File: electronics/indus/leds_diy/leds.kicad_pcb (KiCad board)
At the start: 2 copper layers, 230 x 35.6 mm, 21 parts, among them P1 LED+, P2 THERM, P3 LED-

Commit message: new connector footprint
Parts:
- P1, P3: footprint risebox:PINHEAD_LOCK_1-4 -> risebox:CONNECT_TE_3-647166-4
- P2: footprint risebox:PINHEAD_LOCK_1-3 -> risebox:CONNECT_TE_3-647166-3
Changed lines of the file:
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@@
   )
   (setup
-    (last_trace_width 0.8)
+    (last_trace_width 0.6)
     (user_trace_width 0.3)
     (user_trace_width 0.8)
@@
     )
   )
-  (module risebox:PINHEAD_LOCK_1-4 (layer F.Cu)
-    (at 45.1739 87.7443 270)
-    (attr virtual)
-    (fp_text reference P1 (at 0 -5 270) (layer F.SilkS)
-      (effects (font (size 1 1) (thickness 0.15)))
-    )
-    (fp_text value LED+ (at 0 5 270) (layer F.Fab)
-      (effects (font (size 1 1) (thickness 0.15)))
-    )
-    (fp_line (start -5.04 -1.675) (end 5.04 -1.675) (layer F.SilkS) (width 0.15))
-    (fp_line (start 5.04 2.54) (end -5.04 2.54) (layer F.SilkS) (width 0.15))
-    (fp_line (start -5.04 -3.175) (end 5.04 -3.175) (layer F.SilkS) (width 0.15))
-    (fp_line (start -5.04 -3.175) (end -5.04 2.54) (layer F.SilkS) (width 0.15))
-    (fp_line (start 5.04 -3.175) (end 5.04 2.54) (layer F.SilkS) (width 0.15))
-    (pad 4 thru_hole oval (at 3.77 0 270) (size 1.50622 3.01498) (drill 0.99822) (layers *.Cu *.Mask)
-      (net 8 "Net-(D4-Pad1)"))
-    (pad 3 thru_hole oval (at 1.27 0 270) (size 1.50622 3.01498) (drill 0.99822) (layers *.Cu *.Mask)
-      (net 6 "Net-(D3-Pad1)"))
-    (pad 1 thru_hole oval (at -3.77 0 270) (size 1.50622 3.01498) (drill 0.99822) (layers *.Cu *.Mask)
-      (net 2 "Net-(D1-Pad1)"))
-    (pad 2 thru_hole oval (at -1.23 0 270) (size 1.50622 3.01498) (drill 0.99822) (layers *.Cu *.Mask)
-      (net 4 "Net-(D2-Pad1)"))
-  )
-  (module risebox:PINHEAD_LOCK_1-4 (layer F.Cu)
-    (at 264.12 87.36 270)
-    (attr virtual)
-    (fp_text reference P3 (at 0 -5 270) (layer F.SilkS)
-      (effects (font (size 1 1) (thickness 0.15)))
-    )
-    (fp_text value LED- (at 0 5 270) (layer F.Fab)
-      (effects (font (size 1 1) (thickness 0.15)))
-    )
-    (fp_line (start -5.04 -1.675) (end 5.04 -1.675) (layer F.SilkS) (width 0.15))
-    (fp_line (start 5.04 2.54) (end -5.04 2.54) (layer F.SilkS) (width 0.15))
-    (fp_line (start -5.04 -3.175) (end 5.04 -3.175) (layer F.SilkS) (width 0.15))
-    (fp_line (start -5.04 -3.175) (end -5.04 2.54) (layer F.SilkS) (width 0.15))
-    (fp_line (start 5.04 -3.175) (end 5.04 2.54) (layer F.SilkS) (width 0.15))
-    (pad 4 thru_hole oval (at 3.77 0 270) (size 1.50622 3.01498) (drill 0.99822) (layers *.Cu *.Mask)
-      (net 17 "Net-(D13-Pad2)"))
-    (pad 3 thru_hole oval (at 1.27 0 270) (size 1.50622 3.01498) (drill 0.99822) (layers *.Cu *.Mask)
-      (net 18 "Net-(D14-Pad2)"))
-    (pad 1 thru_hole oval (at -3.77 0 270) (size 1.50622 3.01498) (drill 0.99822) (layers *.Cu *.Mask)
-      (net 20 "Net-(D16-Pad2)"))
-    (pad 2 thru_hole oval (at -1.23 0 270) (size 1.50622 3.01498) (drill 0.99822) (layers *.Cu *.Mask)
-      (net 19 "Net-(D15-Pad2)"))
-  )
   (module risebox:THERM_NTCS0603E3272JMT_SMD0603 (layer F.Cu)
     (at 110 148.9 90)
@@
       (net 21 GND))
   )
-  (module risebox:PINHEAD_LOCK_1-3 (layer F.Cu)
-    (at 74.8 139.4 90)
-    (attr virtual)
-    (fp_text reference P2 (at 0 -5 90) (layer F.SilkS)
-      (effects (font (size 1 1) (thickness 0.15)))
-    )
-    (fp_text value THERM (at 0 5 90) (layer F.Fab)
-      (effects (font (size 1 1) (thickness 0.15)))
-    )
-    (fp_line (start -3.84 -1.675) (end 3.84 -1.675) (layer F.SilkS) (width 0.15))
-    (fp_line (start 3.84 2.54) (end -3.84 2.54) (layer F.SilkS) (width 0.15))
-    (fp_line (start -3.84 -3.175) (end 3.84 -3.175) (layer F.SilkS) (width 0.15))
-    (fp_line (start -3.84 -3.175) (end -3.84 2.54) (layer F.SilkS) (width 0.15))
-    (fp_line (start 3.84 -3.175) (end 3.84 2.54) (layer F.SilkS) (width 0.15))
-    (pad 3 thru_hole oval (at 2.54 0 90) (size 1.50622 3.01498) (drill 0.99822) (layers *.Cu *.Mask)
-      (net 23 "Net-(P2-Pad3)"))
-    (pad 1 thru_hole oval (at -2.54 0 90) (size 1.50622 3.01498) (drill 0.99822) (layers *.Cu *.Mask)
-      (net 21 GND))
-    (pad 2 thru_hole oval (at 0 0 90) (size 1.50622 3.01498) (drill 0.99822) (layers *.Cu *.Mask)
-      (net 22 "Net-(P2-Pad2)"))
-  )
   (module risebox:LUXEON-C (layer F.Cu)
     (at 73.9942 85.4897)
@@
       (net 16 "Net-(D12-Pad2)") (solder_mask_margin 0.05) (solder_paste_margin -0.05))
   )
+  (module risebox:CONNECT_TE_3-647166-4 (layer F.Cu)
+    (at 45.1739 87.7443 270)
+    (fp_text reference P1 (at 0.05 8.4 270) (layer F.SilkS)
+      (effects (font (size 1 1) (thickness 0.15)))
+    )
+    (fp_text value LED+ (at 0.05 -6.7 270) (layer F.Fab)
+      (effects (font (size 1 1) (thickness 0.15)))
+    )
+    (fp_line (start 5.08 -3.175) (end 5.08 3.175) (layer F.SilkS) (width 0.15))
+    (fp_line (start -5.08 -3.175) (end -5.08 3.175) (layer F.SilkS) (width 0.15))
+    (fp_line (start -5.08 3.175) (end 5.08 3.175) (layer F.SilkS) (width 0.15))
+    (fp_line (start -5.08 -3.175) (end 5.08 -3.175) (layer F.SilkS) (width 0.15))
+    (pad 4 smd rect (at 3.81 -1.465 270) (size 1.78 5.97) (layers F.Cu F.Paste F.Mask)
+      (net 8 "Net-(D4-Pad1)"))
+    (pad 1 smd rect (at -3.81 1.465 270) (size 1.78 5.97) (layers F.Cu F.Paste F.Mask)
+      (net 2 "Net-(D1-Pad1)"))
+    (pad 3 smd rect (at 1.27 1.465 270) (size 1.78 5.97) (layers F.Cu F.Paste F.Mask)
+      (net 6 "Net-(D3-Pad1)"))
+    (pad 2 smd rect (at -1.27 -1.465 270) (size 1.78 5.97) (layers F.Cu F.Paste F.Mask)
+      (net 4 "Net-(D2-Pad1)"))
+  )
+  (module risebox:CONNECT_TE_3-647166-3 (layer F.Cu)
+    (at 74.8 139.4 90)
+    (fp_text reference P2 (at 0.05 8.4 90) (layer F.SilkS)
+      (effects (font (size 1 1) (thickness 0.15)))
+    )
+    (fp_text value THERM (at 0.05 -6.7 90) (layer F.Fab)
+      (effects (font (size 1 1) (thickness 0.15)))
+    )
+    (fp_line (start 3.81 -3.175) (end 3.81 3.175) (layer F.SilkS) (width 0.15))
+    (fp_line (start -3.81 -3.175) (end -3.81 3.175) (layer F.SilkS) (width 0.15))
+    (fp_line (start -3.81 3.175) (end 3.81 3.175) (layer F.SilkS) (width 0.15))
+    (fp_line (start -3.81 -3.175) (end 3.81 -3.175) (layer F.SilkS) (width 0.15))
+    (pad 1 smd rect (at -2.54 1.465 90) (size 1.78 5.97) (layers F.Cu F.Paste F.Mask)
+      (net 21 GND))
+    (pad 3 smd rect (at 2.54 1.465 90) (size 1.78 5.97) (layers F.Cu F.Paste F.Mask)
+      (net 23 "Net-(P2-Pad3)"))
+    (pad 2 smd rect (at 0 -1.465 90) (size 1.78 5.97) (layers F.Cu F.Paste F.Mask)
+      (net 22 "Net-(P2-Pad2)"))
+  )
+  (module risebox:CONNECT_TE_3-647166-4 (layer F.Cu)
+    (at 264.12 87.36 270)
+    (fp_text reference P3 (at 0.05 8.4 270) (layer F.SilkS)
+      (effects (font (size 1 1) (thickness 0.15)))
+    )
+    (fp_text value LED- (at 0.05 -6.7 270) (layer F.Fab)
+      (effects (font (size 1 1) (thickness 0.15)))
+    )
+    (fp_line (start 5.08 -3.175) (end 5.08 3.175) (layer F.SilkS) (width 0.15))
+    (fp_line (start -5.08 -3.175) (end -5.08 3.175) (layer F.SilkS) (width 0.15))
+    (fp_line (start -5.08 3.175) (end 5.08 3.175) (layer F.SilkS) (width 0.15))
+    (fp_line (start -5.08 -3.175) (end 5.08 -3.175) (layer F.SilkS) (width 0.15))
+    (pad 4 smd rect (at 3.81 -1.465 270) (size 1.78 5.97) (layers F.Cu F.Paste F.Mask)
+      (net 17 "Net-(D13-Pad2)"))
+    (pad 1 smd rect (at -3.81 1.465 270) (size 1.78 5.97) (layers F.Cu F.Paste F.Mask)
+      (net 20 "Net-(D16-Pad2)"))
+    (pad 3 smd rect (at 1.27 1.465 270) (size 1.78 5.97) (layers F.Cu F.Paste F.Mask)
+      (net 18 "Net-(D14-Pad2)"))
+    (pad 2 smd rect (at -1.27 -1.465 270) (size 1.78 5.97) (layers F.Cu F.Paste F.Mask)
+      (net 19 "Net-(D15-Pad2)"))
+  )
   (gr_line (start 71.2674 87.3984) (end 305.2674 87.3984) (angle 90) (layer F.SilkS) (width 0.2))

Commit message: 2 last LEDs well positioned on PCB
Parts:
- moved D9 55.0 mm to (184.3, 85.4)
- moved D10 50.3 mm to (180.0, 85.4)
- moved D12 49.9 mm to (184.3, 89.7)
- moved D11 48.0 mm to (180.0, 89.7)
- moved D16 32.0 mm to (238.2, 89.6)
- moved D15 23.0 mm to (233.9, 89.7)
- moved D14 14.0 mm to (233.9, 85.4)
- moved D13 5.91 mm to (238.2, 85.4)
- moved P1 0.58 mm to (45.7, 87.5)
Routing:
- net Net-(D2-Pad1): track 24.2 -> 22.4 mm
- net Net-(D3-Pad1): track 29.5 -> 29.0 mm
- net Net-(D1-Pad1): track 32.1 -> 31.6 mm
- net Net-(D4-Pad1): track 25.4 -> 24.9 mm
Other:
- board size 230 x 35.6 mm -> 230 x 35 mm

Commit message: fini routage LEDS
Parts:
- moved TH1 92.0 mm to (52.8, 76.9)
- moved R1 88.3 mm to (50.5, 71.6), turned to 0 degrees
- moved P2 68.9 mm to (45.7, 77.0)
- moved D12 4.31 mm to (180.0, 89.7)
- moved D11 4.30 mm to (184.3, 89.7)
- moved D16 4.30 mm to (233.9, 89.6)
- moved D15 4.28 mm to (238.2, 89.6)
- turned P3 to 90 degrees
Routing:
- net Net-(D13-Pad1): track 0.00 -> 56.0 mm
- net Net-(D12-Pad2): track 0.00 -> 55.9 mm
- net Net-(D11-Pad2): track 0.00 -> 54.5 mm
- net Net-(D10-Pad2): track 0.00 -> 54.2 mm
- net Net-(D11-Pad1): track 6.46 -> 53.5 mm
- net Net-(D5-Pad2): track 7.43 -> 54.2 mm
- net Net-(D12-Pad1): track 12.9 -> 55.3 mm
- net Net-(D10-Pad1): track 12.7 -> 53.9 mm
- net Net-(D16-Pad2): track 0.00 -> 33.5 mm
- net Net-(D14-Pad2): track 0.00 -> 32.1 mm
- net Net-(D13-Pad2): track 0.00 -> 24.5 mm
- net Net-(D15-Pad2): track 0.00 -> 24.2 mm
- net Net-(P2-Pad2): track 0.00 -> 13.9 mm
- net GND: track 0.00 -> 6.34 mm
- net Net-(P2-Pad3): track 0.00 -> 3.80 mm

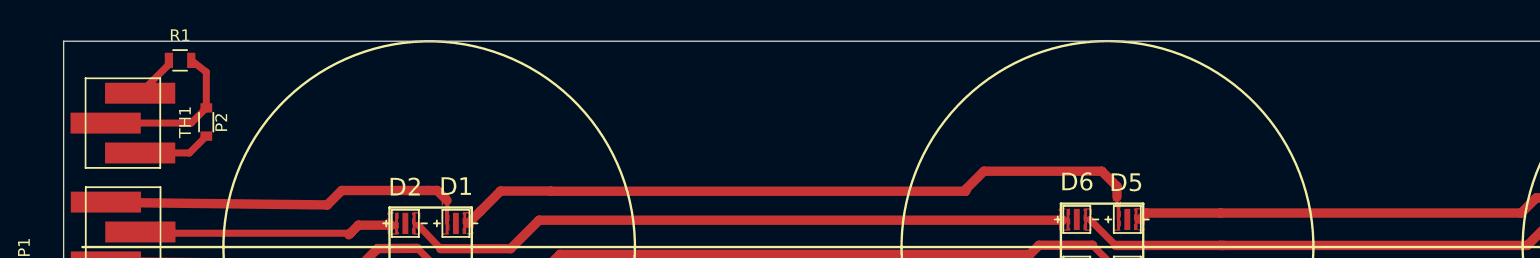
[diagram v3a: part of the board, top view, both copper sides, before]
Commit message: new position for connectors
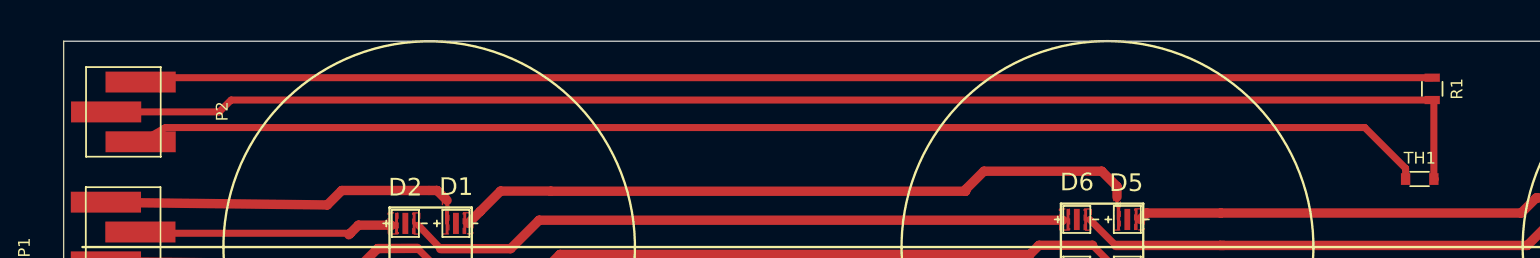
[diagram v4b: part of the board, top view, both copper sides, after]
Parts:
- moved R1 106.5 mm to (157.0, 74.0), turned to 270 degrees
- moved TH1 103.3 mm to (155.9, 81.7), turned to 0 degrees
- moved P2 0.95 mm to (45.7, 76.0)
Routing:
- net Net-(P2-Pad2): track 13.9 -> 120.1 mm
- net Net-(P2-Pad3): track 3.80 -> 110.0 mm
- net GND: track 6.34 -> 110.4 mm
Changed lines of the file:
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@@
     (thickness 1.6)
     (drawings 28)
-    (tracks 188)
+    (tracks 190)
     (zones 0)
     (modules 21)
@@
     (mod_text_size 1 1)
     (mod_text_width 0.15)
-    (pad_size 0.5 1.8)
+    (pad_size 1.78 5.97)
     (pad_drill 0)
     (pad_to_mask_clearance 0)
@@
   )
   (module Resistors_SMD:R_0805 (layer F.Cu)
-    (at 50.54 71.63)
+    (at 157 74.05 270)
     (descr "Resistor SMD 0805, reflow soldering, Vishay (see dcrcw.pdf)")
     (tags "resistor 0805")
     (attr smd)
-    (fp_text reference R1 (at 0 -2.1) (layer F.SilkS)
-      (effects (font (size 1 1) (thickness 0.15)))
-    )
-    (fp_text value 2.7K (at 0 2.1) (layer F.Fab)
+    (fp_text reference R1 (at 0 -2.1 270) (layer F.SilkS)
+      (effects (font (size 1 1) (thickness 0.15)))
+    )
+    (fp_text value 2.7K (at 0 2.1 270) (layer F.Fab)
       (effects (font (size 1 1) (thickness 0.15)))
     )
@@
     (fp_line (start 0.6 0.875) (end -0.6 0.875) (layer F.SilkS) (width 0.15))
     (fp_line (start -0.6 -0.875) (end 0.6 -0.875) (layer F.SilkS) (width 0.15))
-    (pad 1 smd rect (at -0.95 0) (size 0.7 1.3) (layers F.Cu F.Paste F.Mask)
+    (pad 1 smd rect (at -0.95 0 270) (size 0.7 1.3) (layers F.Cu F.Paste F.Mask)
       (net 23 "Net-(P2-Pad3)"))
-    (pad 2 smd rect (at 0.95 0) (size 0.7 1.3) (layers F.Cu F.Paste F.Mask)
+    (pad 2 smd rect (at 0.95 0 270) (size 0.7 1.3) (layers F.Cu F.Paste F.Mask)
       (net 22 "Net-(P2-Pad2)"))
     (model Resistors_SMD.3dshapes/R_0805.wrl
@@
   )
   (module risebox:THERM_NTCS0603E3272JMT_SMD0603 (layer F.Cu)
-    (at 52.77 76.87 90)
-    (fp_text reference TH1 (at 0 -1.778 90) (layer F.SilkS)
-      (effects (font (size 1 1) (thickness 0.15)))
-    )
-    (fp_text value NTCS0603E3272JMT (at 0 1.8796 90) (layer F.Fab)
+    (at 155.94 81.72)
+    (fp_text reference TH1 (at 0 -1.778) (layer F.SilkS)
+      (effects (font (size 1 1) (thickness 0.15)))
+    )
+    (fp_text value NTCS0603E3272JMT (at 0 1.8796) (layer F.Fab)
       (effects (font (size 1 1) (thickness 0.15)))
     )
     (fp_line (start -0.8128 -0.6176) (end 0.7872 -0.6176) (layer F.SilkS) (width 0.15))
     (fp_line (start -0.8128 0.6016) (end 0.7872 0.6016) (layer F.SilkS) (width 0.15))
-    (pad 2 smd rect (at 1.2 0 90) (size 0.8 1) (layers F.Cu F.Paste F.Mask)
+    (pad 2 smd rect (at 1.2 0) (size 0.8 1) (layers F.Cu F.Paste F.Mask)
       (net 22 "Net-(P2-Pad2)"))
-    (pad 1 smd rect (at -1.2 0 90) (size 0.8 1) (layers F.Cu F.Paste F.Mask)
+    (pad 1 smd rect (at -1.2 0) (size 0.8 1) (layers F.Cu F.Paste F.Mask)
       (net 21 GND))
   )
@@
   )
   (module risebox:CONNECT_TE_3-647166-3 (layer F.Cu)
-    (at 45.68 76.96 90)
+    (at 45.72 76.01 90)
     (fp_text reference P2 (at 0.05 8.4 90) (layer F.SilkS)
       (effects (font (size 1 1) (thickness 0.15)))
@@
   (segment (start 243.44 91.17) (end 241.88 92.73) (width 0.8) (layer F.Cu) (net 20))
   (segment (start 234.64 90) (end 234.64 89.64) (width 0.3) (layer F.Cu) (net 20))
-  (segment (start 47.145 79.5) (end 51.34 79.5) (width 0.6) (layer F.Cu) (net 21))
-  (segment (start 51.34 79.5) (end 52.77 78.07) (width 0.6) (layer F.Cu) (net 21))
-  (segment (start 47.235 79.41) (end 47.145 79.5) (width 0.6) (layer F.Cu) (net 21))
-  (segment (start 52.77 75.67) (end 52.77 72.62) (width 0.6) (layer F.Cu) (net 22))
-  (segment (start 52.77 72.62) (end 51.49 71.63) (width 0.6) (layer F.Cu) (net 22) (status 20))
-  (segment (start 44.215 76.96) (end 51.48 76.96) (width 0.6) (layer F.Cu) (net 22))
-  (segment (start 51.48 76.96) (end 52.77 75.67) (width 0.6) (layer F.Cu) (net 22))
-  (segment (start 52.77 75.67) (end 52.77 75.53) (width 0.6) (layer F.Cu) (net 22) (status 30))
-  (segment (start 49.59 71.63) (end 49.53 72.035) (width 0.6) (layer F.Cu) (net 23) (status 10))
-  (segment (start 49.53 72.035) (end 47.145 74.42) (width 0.6) (layer F.Cu) (net 23))
-  (segment (start 49.58 71.64) (end 49.59 71.63) (width 0.3) (layer F.Cu) (net 23) (status 30))
+  (segment (start 154.74 81.72) (end 154.74 80.81) (width 0.6) (layer F.Cu) (net 21))
+  (segment (start 49.305 77.34) (end 47.185 78.55) (width 0.6) (layer F.Cu) (net 21) (status 20))
+  (segment (start 151.27 77.34) (end 49.305 77.34) (width 0.6) (layer F.Cu) (net 21))
+  (segment (start 154.74 80.81) (end 151.27 77.34) (width 0.6) (layer F.Cu) (net 21))
+  (segment (start 47.275 78.46) (end 47.185 78.55) (width 0.6) (layer F.Cu) (net 21) (status 30))
+  (segment (start 157 75) (end 54.88 75) (width 0.6) (layer F.Cu) (net 22) (status 400000))
+  (segment (start 53.87 76.01) (end 44.255 76.01) (width 0.6) (layer F.Cu) (net 22) (status 800000))
+  (segment (start 54.88 75) (end 53.87 76.01) (width 0.6) (layer F.Cu) (net 22))
+  (segment (start 157.14 81.72) (end 157.14 75.14) (width 0.6) (layer F.Cu) (net 22) (status C00000))
+  (segment (start 157.14 75.14) (end 157 75) (width 0.6) (layer F.Cu) (net 22) (status C00000))
+  (segment (start 157.14 81.72) (end 157.28 81.72) (width 0.6) (layer F.Cu) (net 22) (status 30))
+  (segment (start 157 73.1) (end 47.555 73.1) (width 0.6) (layer F.Cu) (net 23) (status C00000))
+  (segment (start 47.555 73.1) (end 47.185 73.47) (width 0.6) (layer F.Cu) (net 23) (status C00000))
   (zone (net 4) (net_name "Net-(D2-Pad1)") (layer F.Cu) (hatch edge 0.508)
     (connect_pads (clearance 0.508))

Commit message: nouvelle position sonde
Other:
- net class Default: clearance 0.8 -> 0.3
- rule trace_clearance: 0.8 -> 0.3
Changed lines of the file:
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@@
     (links 24)
     (no_connects 0)
-    (area 35.575 67.805 276.335201 105.179185)
+    (area 35.575 69.820815 276.335201 105.179185)
     (thickness 1.6)
     (drawings 28)
@@
     (user_trace_width 0.3)
     (user_trace_width 0.8)
-    (trace_clearance 0.8)
+    (trace_clearance 0.3)
     (zone_clearance 0.508)
     (zone_45_only no)
@@
   (net 23 "Net-(P2-Pad3)")
   (net_class Default "This is the default net class."
-    (clearance 0.8)
+    (clearance 0.3)
     (trace_width 0.6)
     (via_dia 0.889)
@@
   (segment (start 154.74 80.81) (end 151.27 77.34) (width 0.6) (layer F.Cu) (net 21))
   (segment (start 47.275 78.46) (end 47.185 78.55) (width 0.6) (layer F.Cu) (net 21) (status 30))
-  (segment (start 157 75) (end 54.88 75) (width 0.6) (layer F.Cu) (net 22) (status 400000))
-  (segment (start 53.87 76.01) (end 44.255 76.01) (width 0.6) (layer F.Cu) (net 22) (status 800000))
+  (segment (start 157 75) (end 54.88 75) (width 0.6) (layer F.Cu) (net 22))
+  (segment (start 53.87 76.01) (end 44.255 76.01) (width 0.6) (layer F.Cu) (net 22))
   (segment (start 54.88 75) (end 53.87 76.01) (width 0.6) (layer F.Cu) (net 22))
-  (segment (start 157.14 81.72) (end 157.14 75.14) (width 0.6) (layer F.Cu) (net 22) (status C00000))
-  (segment (start 157.14 75.14) (end 157 75) (width 0.6) (layer F.Cu) (net 22) (status C00000))
+  (segment (start 157.14 81.72) (end 157.14 75.14) (width 0.6) (layer F.Cu) (net 22))
+  (segment (start 157.14 75.14) (end 157 75) (width 0.6) (layer F.Cu) (net 22))
   (segment (start 157.14 81.72) (end 157.28 81.72) (width 0.6) (layer F.Cu) (net 22) (status 30))
-  (segment (start 157 73.1) (end 47.555 73.1) (width 0.6) (layer F.Cu) (net 23) (status C00000))
-  (segment (start 47.555 73.1) (end 47.185 73.47) (width 0.6) (layer F.Cu) (net 23) (status C00000))
+  (segment (start 157 73.1) (end 47.555 73.1) (width 0.6) (layer F.Cu) (net 23))
+  (segment (start 47.555 73.1) (end 47.185 73.47) (width 0.6) (layer F.Cu) (net 23))
   (zone (net 4) (net_name "Net-(D2-Pad1)") (layer F.Cu) (hatch edge 0.508)
     (connect_pads (clearance 0.508))
